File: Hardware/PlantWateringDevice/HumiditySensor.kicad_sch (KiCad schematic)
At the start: 16 parts, among them J4 Conn_01x03_Socket, U2 LM2903

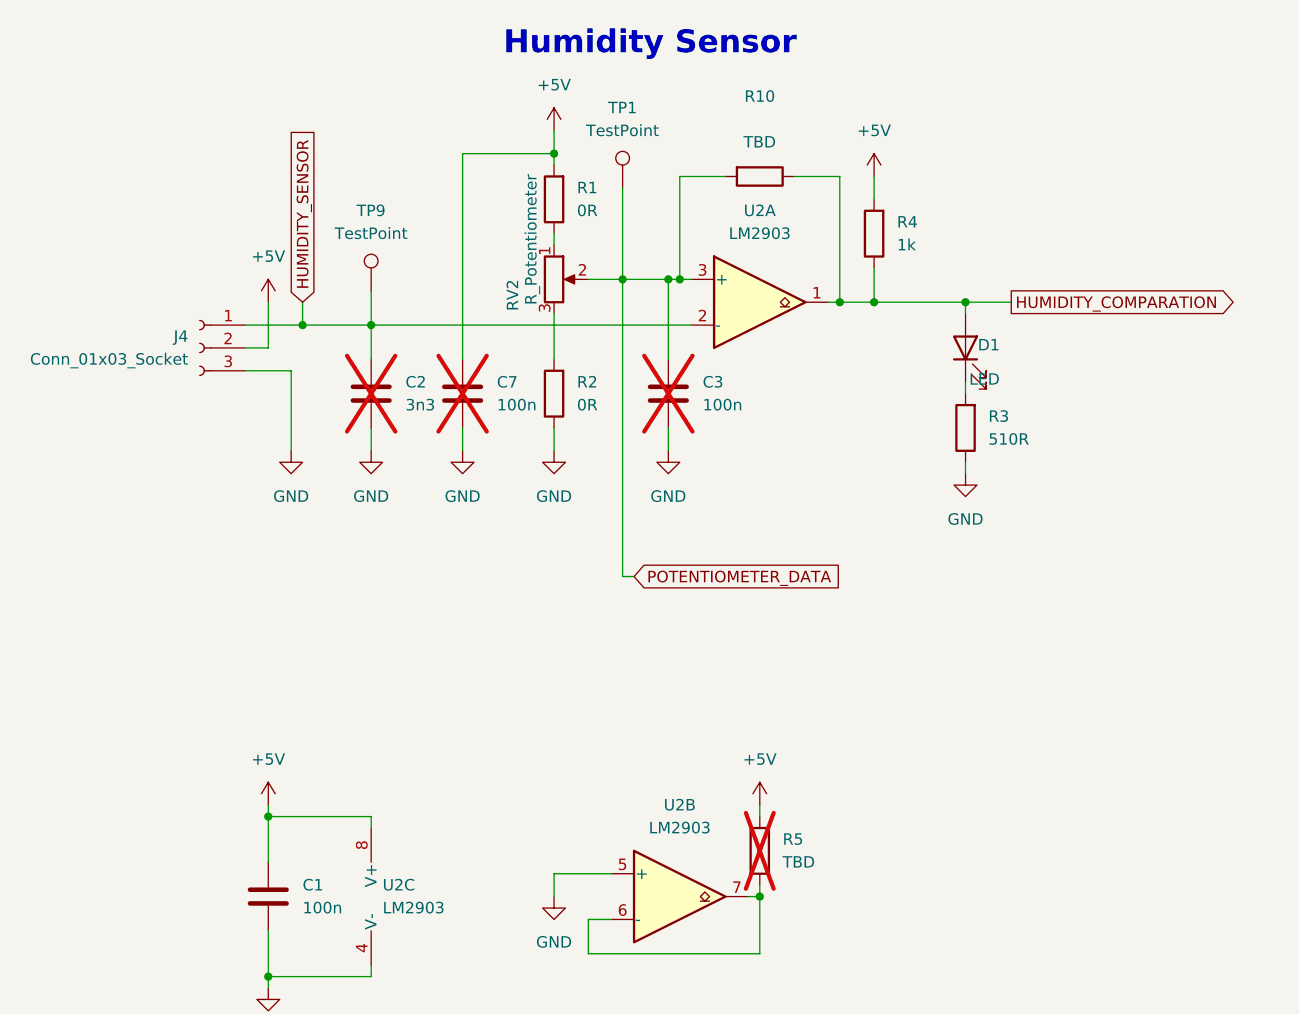
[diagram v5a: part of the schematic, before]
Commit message: hierarchical block diagram structure in kicad
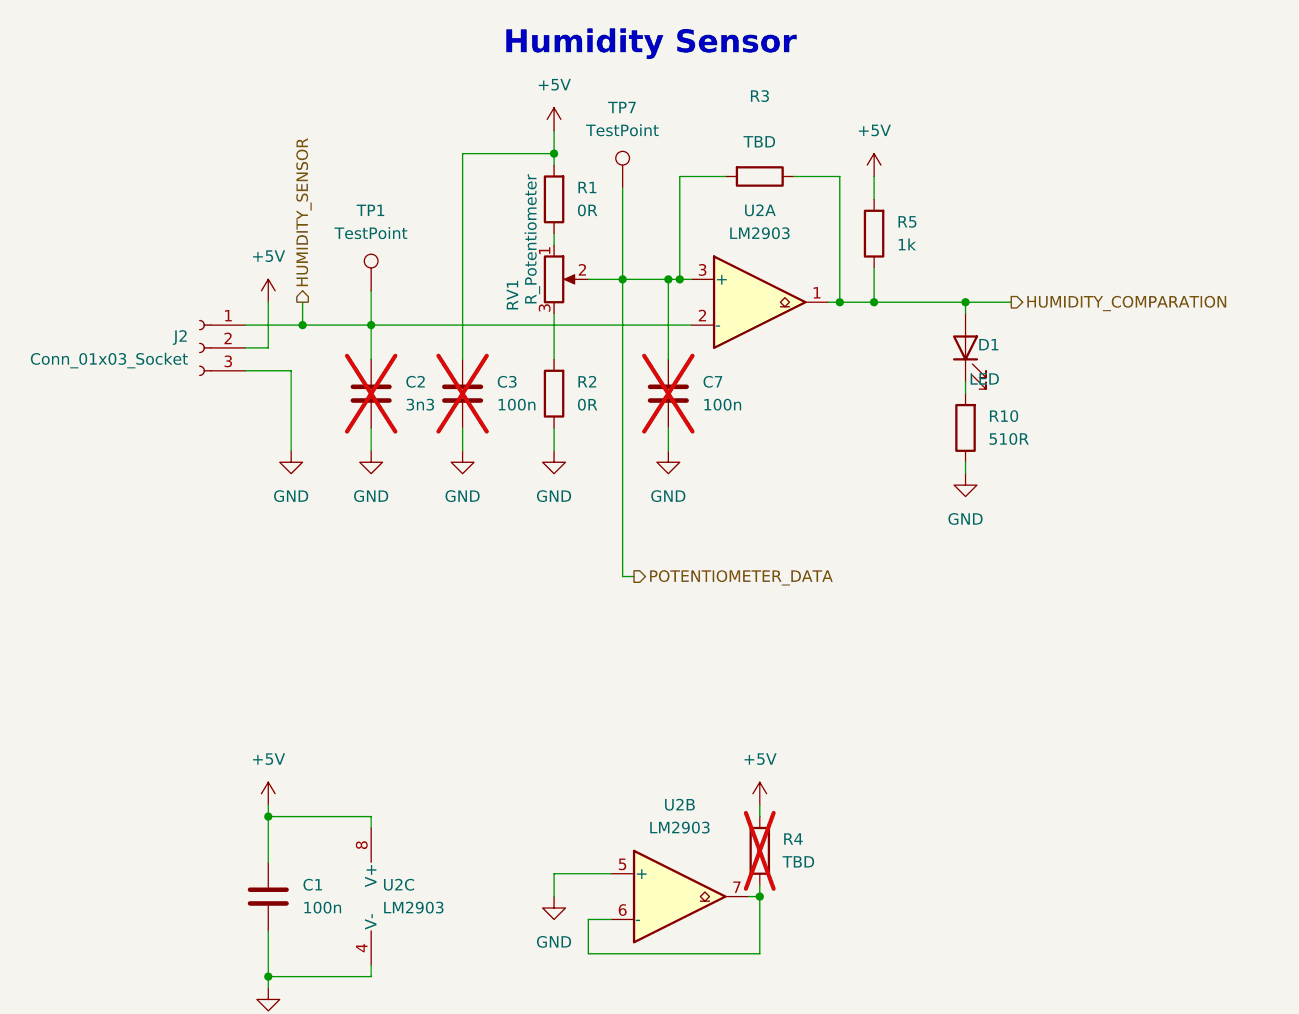
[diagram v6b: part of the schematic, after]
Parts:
- renumbered C7 to C3, C3 to C7, J4 to J2, R3 to R10, R10 to R3, R5 to R4, R4 to R5, RV2 to RV1, TP9 to TP1, TP1 to TP7
